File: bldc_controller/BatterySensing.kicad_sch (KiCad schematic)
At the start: 3 parts

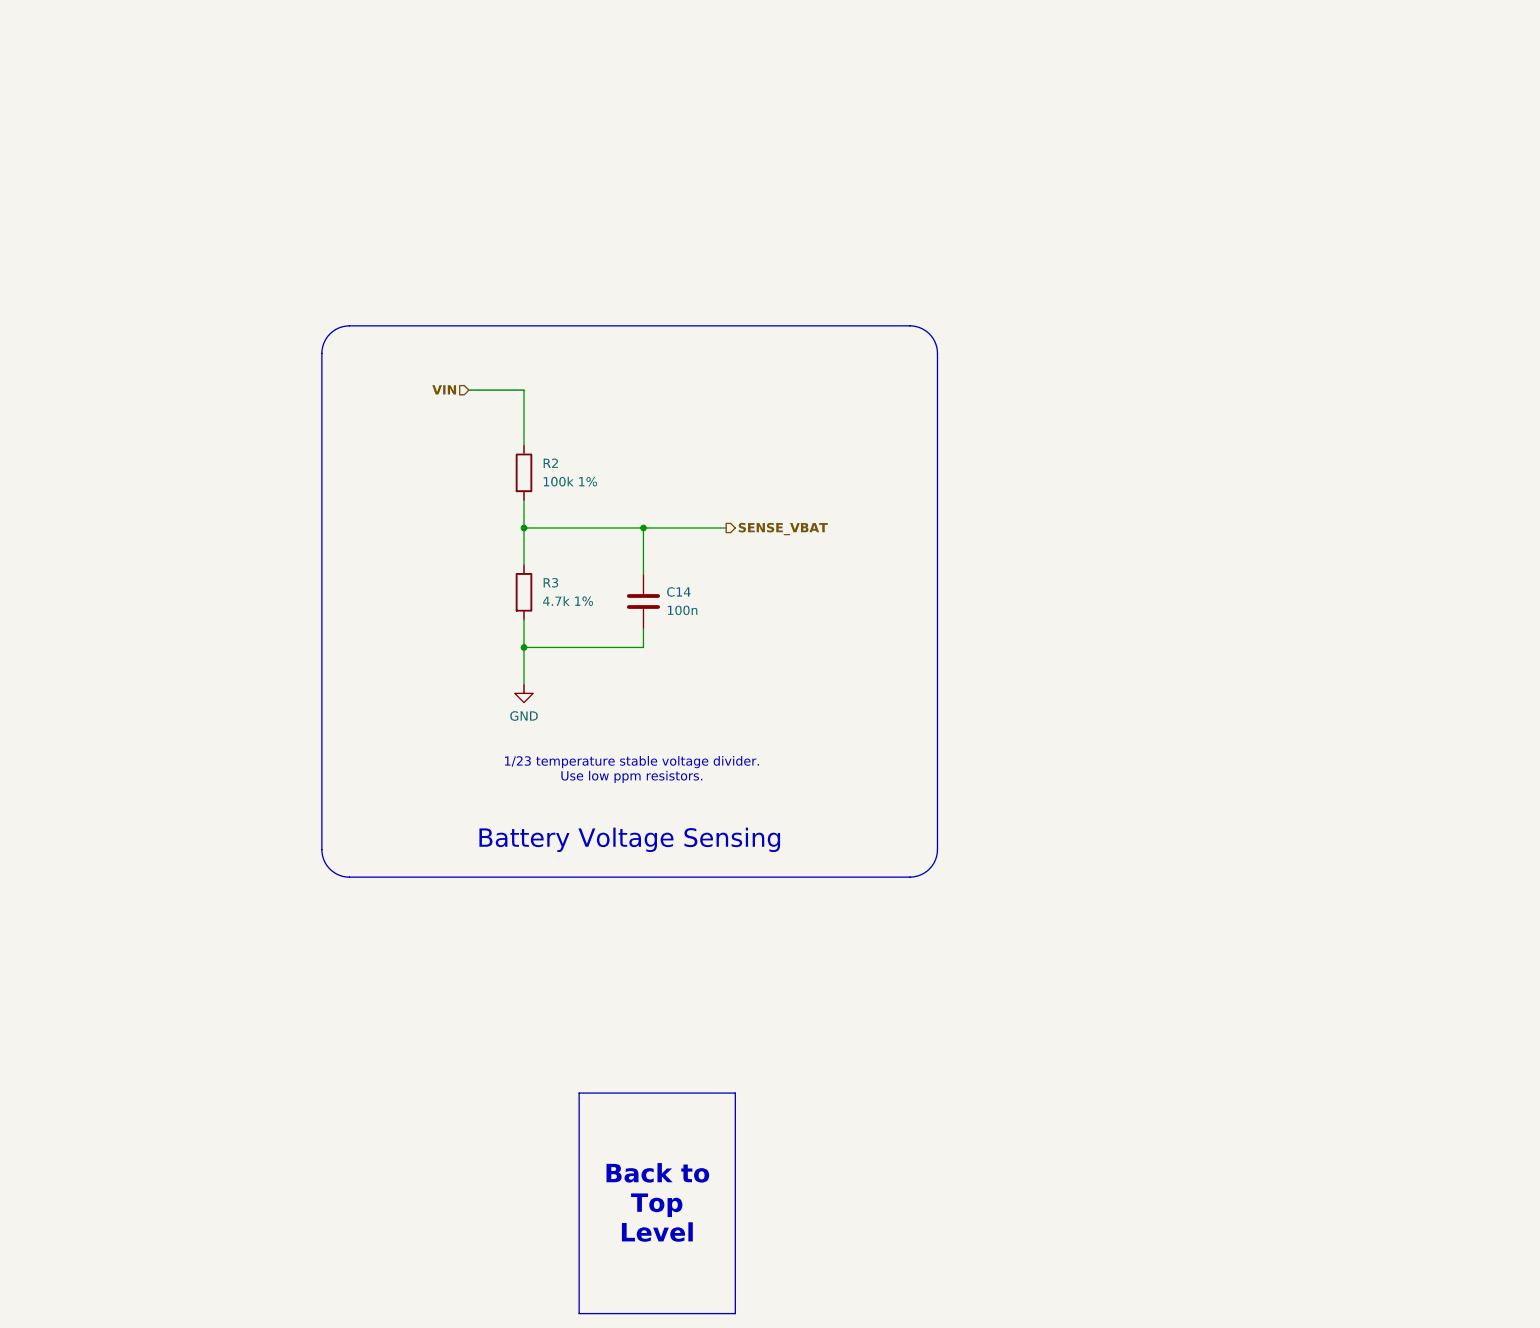
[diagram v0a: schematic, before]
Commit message: added temporary footprints and deleted extra files
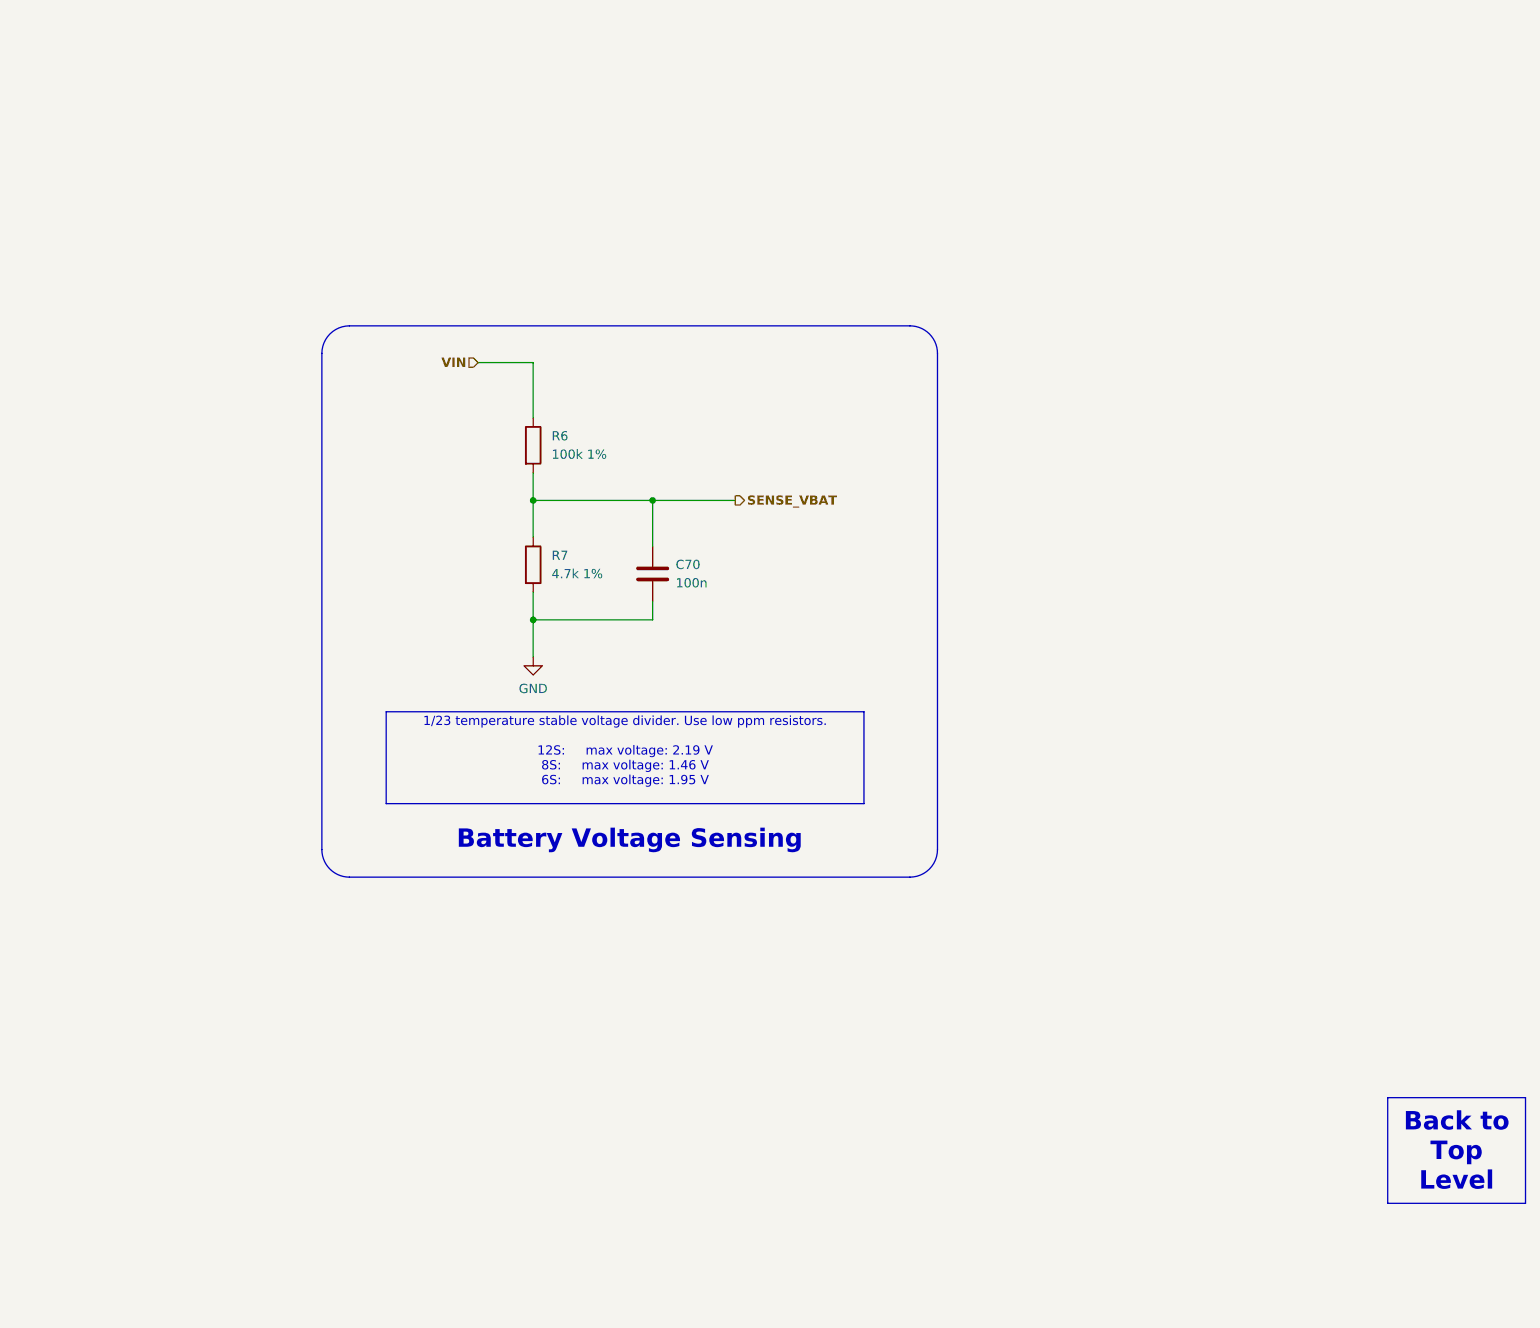
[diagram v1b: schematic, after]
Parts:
- C70: renamed from C14; footprint (none) -> Capacitor_SMD:C_0402_1005Metric
- R6: renamed from R2; footprint (none) -> Resistor_SMD:R_0402_1005Metric
- R7: renamed from R3; footprint (none) -> Resistor_SMD:R_0402_1005Metric
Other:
- moved on the sheet: C70, R6, R7
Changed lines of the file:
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@@
     (comment 3 "Author: Vincent Nguyen")
   )
-  (junction (at 146.05 87.63) (diameter 0) (color 0 0 0 0)
+  (junction (at 147.32 83.82) (diameter 0) (color 0 0 0 0)
   )
-  (junction (at 162.56 87.63) (diameter 0) (color 0 0 0 0)
+  (junction (at 163.83 83.82) (diameter 0) (color 0 0 0 0)
   )
-  (junction (at 146.05 104.14) (diameter 0) (color 0 0 0 0)
+  (junction (at 147.32 100.33) (diameter 0) (color 0 0 0 0)
   )
   (polyline (pts (xy 118.11 63.5) (xy 118.11 132.08))
     (stroke (width 0) (type default))
   )
-  (wire (pts (xy 162.56 87.63) (xy 162.56 93.98))
+  (wire (pts (xy 163.83 83.82) (xy 163.83 90.17))
     (stroke (width 0) (type default))
   )
-  (wire (pts (xy 162.56 87.63) (xy 146.05 87.63))
+  (wire (pts (xy 163.83 83.82) (xy 147.32 83.82))
     (stroke (width 0) (type default))
   )
-  (wire (pts (xy 162.56 101.6) (xy 162.56 104.14))
+  (wire (pts (xy 163.83 97.79) (xy 163.83 100.33))
     (stroke (width 0) (type default))
   )
@@
     (stroke (width 0) (type default))
   )
-  (wire (pts (xy 146.05 87.63) (xy 146.05 92.71))
+  (wire (pts (xy 147.32 83.82) (xy 147.32 88.9))
     (stroke (width 0) (type default))
   )
-  (wire (pts (xy 162.56 104.14) (xy 146.05 104.14))
+  (wire (pts (xy 163.83 100.33) (xy 147.32 100.33))
     (stroke (width 0) (type default))
   )
-  (wire (pts (xy 146.05 68.58) (xy 146.05 76.2))
+  (wire (pts (xy 147.32 64.77) (xy 147.32 72.39))
+    (stroke (width 0.381) (type default) (color 200 50 50 1))
+  )
+  (wire (pts (xy 163.83 83.82) (xy 175.26 83.82))
     (stroke (width 0) (type default))
   )
-  (wire (pts (xy 162.56 87.63) (xy 173.99 87.63))
+  (wire (pts (xy 147.32 80.01) (xy 147.32 83.82))
     (stroke (width 0) (type default))
   )
-  (wire (pts (xy 146.05 83.82) (xy 146.05 87.63))
+  (wire (pts (xy 139.7 64.77) (xy 147.32 64.77))
+    (stroke (width 0.381) (type default) (color 200 50 50 1))
+  )
+  (wire (pts (xy 147.32 105.41) (xy 147.32 100.33))
     (stroke (width 0) (type default))
   )
-  (wire (pts (xy 138.43 68.58) (xy 146.05 68.58))
-    (stroke (width 0) (type default))
-  )
-  (wire (pts (xy 146.05 109.22) (xy 146.05 104.14))
-    (stroke (width 0) (type default))
-  )
-  (wire (pts (xy 146.05 104.14) (xy 146.05 100.33))
+  (wire (pts (xy 147.32 100.33) (xy 147.32 96.52))
     (stroke (width 0) (type default))
   )
@@
     (fill (type none))
   )
+  (text_box "Back to Top Level"
+    (at 265.43 166.37 0) (size 19.05 14.605)
+    (stroke (width 0) (type default) (color 0 0 0 1))
+    (fill (type color) (color 0 0 0 0.1))
+    (effects (font (size 2.54 2.54) (thickness 0.508) bold (color 0 0 0 1)) (href "#1"))
+  )
   (text_box "Battery Voltage Sensing"
     (at 120.015 124.46 0) (size 81.28 9.525)
     (stroke (width -0.0001) (type default))
     (fill (type none))
-    (effects (font (size 2.54 2.54) (color 0 0 0 1)) (justify bottom))
+    (effects (font (size 2.54 2.54) (thickness 0.508) bold (color 0 0 0 1)) (justify bottom))
   )
-  (text_box "1/23 temperature stable voltage divider. Use low ppm resistors.\n"
-    (at 138.43 118.11 0) (size 45.085 8.255)
-    (stroke (width -0.0001) (type default))
-    (fill (type none))
-    (effects (font (size 1.27 1.27)) (justify top))
+  (text_box "1/23 temperature stable voltage divider. Use low ppm resistors.\n\n12S: 	max voltage: 2.19 V\n8S: 	max voltage: 1.46 V\n6S: 	max voltage: 1.95 V\n\n"
+    (at 127 113.03 0) (size 66.04 12.7)
+    (stroke (width 0) (type default) (color 0 0 0 1))
+    (fill (type color) (color 191 240 255 1))
+    (effects (font (size 1.27 1.27) (color 0 0 0 1)))
   )
-  (text_box "Back to Top Level"
-    (at 153.67 165.735 0) (size 21.59 30.48)
-    (stroke (width 0) (type default) (color 0 0 0 1))
-    (fill (type color) (color 0 0 0 0.1))
-    (effects (font (size 2.54 2.54) (thickness 0.508) bold (color 0 0 0 1)) (href "#1"))
-  )
-  (hierarchical_label "VIN" (shape input) (at 138.43 68.58 180) (fields_autoplaced)
+  (hierarchical_label "VIN" (shape input) (at 139.7 64.77 180) (fields_autoplaced)
     (effects (font (size 1.27 1.27) bold) (justify right))
   )
-  (hierarchical_label "SENSE_VBAT" (shape output) (at 173.99 87.63 0) (fields_autoplaced)
+  (hierarchical_label "SENSE_VBAT" (shape output) (at 175.26 83.82 0) (fields_autoplaced)
     (effects (font (size 1.27 1.27) bold) (justify left))
   )
-  (symbol (lib_id "Device:R") (at 146.05 96.52 0) (unit 1)
+  (symbol (lib_id "Device:R") (at 147.32 92.71 0) (unit 1)
     (in_bom yes) (on_board yes) (dnp no) (fields_autoplaced)
-    (property "Reference" "R3" (at 148.59 95.25 0)
+    (property "Reference" "R7" (at 149.86 91.44 0)
       (effects (font (size 1.27 1.27)) (justify left))
     )
-    (property "Value" "4.7k 1%" (at 148.59 97.79 0)
+    (property "Value" "4.7k 1%" (at 149.86 93.98 0)
       (effects (font (size 1.27 1.27)) (justify left))
     )
-    (property "Footprint" "" (at 144.272 96.52 90)
+    (property "Footprint" "Resistor_SMD:R_0402_1005Metric" (at 145.542 92.71 90)
       (effects (font (size 1.27 1.27)) hide)
     )
-    (property "Datasheet" "~" (at 146.05 96.52 0)
+    (property "Datasheet" "~" (at 147.32 92.71 0)
       (effects (font (size 1.27 1.27)) hide)
     )
@@
       (project "bldc_controller"
         (path "/0650c7a8-acba-429c-9f8e-eec0baf0bc1c/7fc64539-f083-49cd-b390-cfa281750e68"
-          (reference "R3") (unit 1)
+          (reference "R7") (unit 1)
         )
       )
     )
   )
-  (symbol (lib_id "Device:C") (at 162.56 97.79 0) (unit 1)
+  (symbol (lib_id "Device:C") (at 163.83 93.98 0) (unit 1)
     (in_bom yes) (on_board yes) (dnp no) (fields_autoplaced)
-    (property "Reference" "C14" (at 165.735 96.52 0)
+    (property "Reference" "C70" (at 167.005 92.71 0)
       (effects (font (size 1.27 1.27)) (justify left))
     )
-    (property "Value" "100n" (at 165.735 99.06 0)
+    (property "Value" "100n" (at 167.005 95.25 0)
       (effects (font (size 1.27 1.27)) (justify left))
     )
-    (property "Footprint" "" (at 163.5252 101.6 0)
+    (property "Footprint" "Capacitor_SMD:C_0402_1005Metric" (at 164.7952 97.79 0)
       (effects (font (size 1.27 1.27)) hide)
     )
-    (property "Datasheet" "~" (at 162.56 97.79 0)
+    (property "Datasheet" "~" (at 163.83 93.98 0)
       (effects (font (size 1.27 1.27)) hide)
     )
@@
       (project "bldc_controller"
         (path "/0650c7a8-acba-429c-9f8e-eec0baf0bc1c/7fc64539-f083-49cd-b390-cfa281750e68"
-          (reference "C14") (unit 1)
+          (reference "C70") (unit 1)
         )
       )
     )
   )
-  (symbol (lib_id "power:GND") (at 146.05 109.22 0) (unit 1)
+  (symbol (lib_id "power:GND") (at 147.32 105.41 0) (unit 1)
     (in_bom yes) (on_board yes) (dnp no) (fields_autoplaced)
-    (property "Reference" "#PWR016" (at 146.05 115.57 0)
+    (property "Reference" "#PWR021" (at 147.32 111.76 0)
       (effects (font (size 1.27 1.27)) hide)
     )
-    (property "Value" "GND" (at 146.05 113.665 0)
+    (property "Value" "GND" (at 147.32 109.855 0)
       (effects (font (size 1.27 1.27)))
     )
-    (property "Footprint" "" (at 146.05 109.22 0)
+    (property "Footprint" "" (at 147.32 105.41 0)
       (effects (font (size 1.27 1.27)) hide)
     )
-    (property "Datasheet" "" (at 146.05 109.22 0)
+    (property "Datasheet" "" (at 147.32 105.41 0)
       (effects (font (size 1.27 1.27)) hide)
     )
@@
       (project "bldc_controller"
         (path "/0650c7a8-acba-429c-9f8e-eec0baf0bc1c/7fc64539-f083-49cd-b390-cfa281750e68"
-          (reference "#PWR016") (unit 1)
+          (reference "#PWR021") (unit 1)
         )
       )
     )
   )
-  (symbol (lib_id "Device:R") (at 146.05 80.01 0) (unit 1)
+  (symbol (lib_id "Device:R") (at 147.32 76.2 0) (unit 1)
     (in_bom yes) (on_board yes) (dnp no) (fields_autoplaced)
-    (property "Reference" "R2" (at 148.59 78.74 0)
+    (property "Reference" "R6" (at 149.86 74.93 0)
       (effects (font (size 1.27 1.27)) (justify left))
     )
-    (property "Value" "100k 1%" (at 148.59 81.28 0)
+    (property "Value" "100k 1%" (at 149.86 77.47 0)
       (effects (font (size 1.27 1.27)) (justify left))
     )
-    (property "Footprint" "" (at 144.272 80.01 90)
+    (property "Footprint" "Resistor_SMD:R_0402_1005Metric" (at 145.542 76.2 90)
       (effects (font (size 1.27 1.27)) hide)
     )
-    (property "Datasheet" "~" (at 146.05 80.01 0)
+    (property "Datasheet" "~" (at 147.32 76.2 0)
       (effects (font (size 1.27 1.27)) hide)
     )
@@
       (project "bldc_controller"
         (path "/0650c7a8-acba-429c-9f8e-eec0baf0bc1c/7fc64539-f083-49cd-b390-cfa281750e68"
-          (reference "R2") (unit 1)
+          (reference "R6") (unit 1)
         )
       )

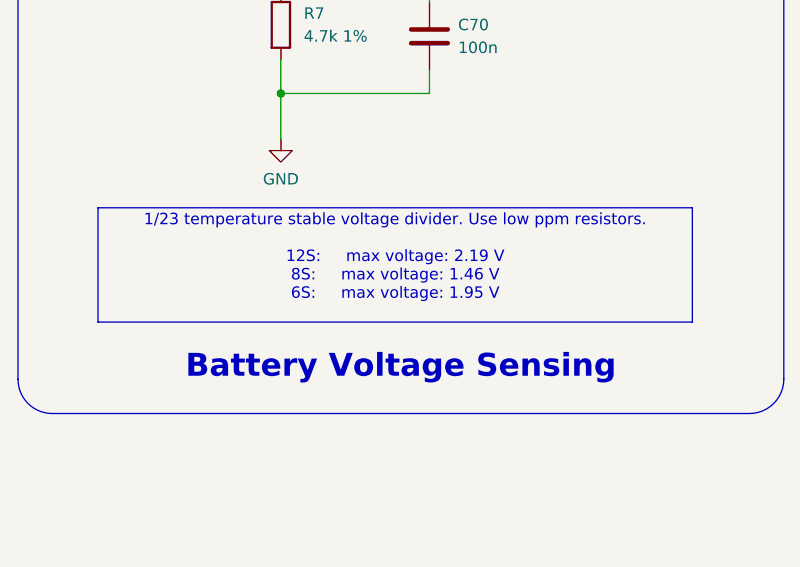
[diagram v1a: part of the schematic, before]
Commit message: added IPC-7351 compliant footprints and started routing
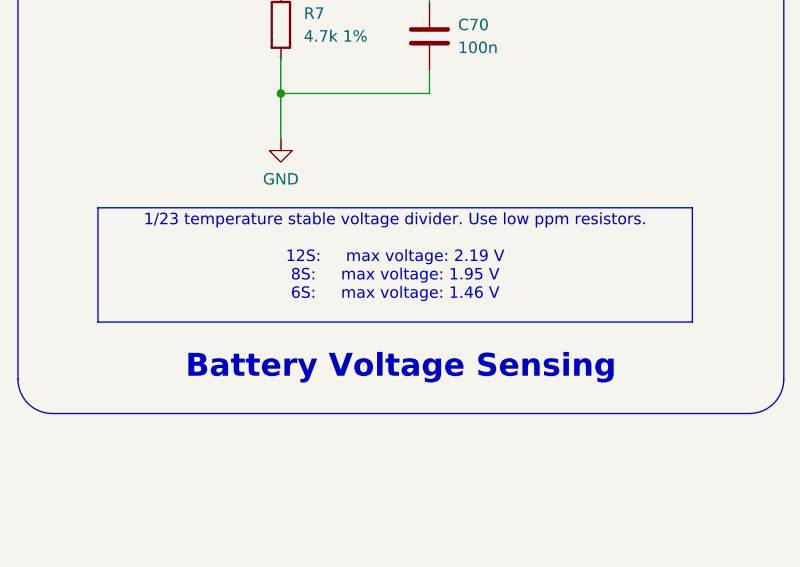
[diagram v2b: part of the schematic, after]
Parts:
- C70: footprint Capacitor_SMD:C_0402_1005Metric -> 0_capacitor_smd:C_0402_1005_DensityHigh
- R6, R7: footprint Resistor_SMD:R_0402_1005Metric -> 0_resistor_smd:R_0402_1005_DensityHigh
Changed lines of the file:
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@@
     (effects (font (size 2.54 2.54) (thickness 0.508) bold (color 0 0 0 1)) (justify bottom))
   )
-  (text_box "1/23 temperature stable voltage divider. Use low ppm resistors.\n\n12S: 	max voltage: 2.19 V\n8S: 	max voltage: 1.46 V\n6S: 	max voltage: 1.95 V\n\n"
+  (text_box "1/23 temperature stable voltage divider. Use low ppm resistors.\n\n12S: 	max voltage: 2.19 V\n8S: 	max voltage: 1.95 V\n6S: 	max voltage: 1.46 V\n\n"
     (at 127 113.03 0) (size 66.04 12.7)
     (stroke (width 0) (type default) (color 0 0 0 1))
@@
       (effects (font (size 1.27 1.27)) (justify left))
     )
-    (property "Footprint" "Resistor_SMD:R_0402_1005Metric" (at 145.542 92.71 90)
+    (property "Footprint" "0_resistor_smd:R_0402_1005_DensityHigh" (at 145.542 92.71 90)
       (effects (font (size 1.27 1.27)) hide)
     )
@@
       (effects (font (size 1.27 1.27)) (justify left))
     )
-    (property "Footprint" "Capacitor_SMD:C_0402_1005Metric" (at 164.7952 97.79 0)
+    (property "Footprint" "0_capacitor_smd:C_0402_1005_DensityHigh" (at 164.7952 97.79 0)
       (effects (font (size 1.27 1.27)) hide)
     )
@@
       (effects (font (size 1.27 1.27)) (justify left))
     )
-    (property "Footprint" "Resistor_SMD:R_0402_1005Metric" (at 145.542 76.2 90)
+    (property "Footprint" "0_resistor_smd:R_0402_1005_DensityHigh" (at 145.542 76.2 90)
       (effects (font (size 1.27 1.27)) hide)
     )
